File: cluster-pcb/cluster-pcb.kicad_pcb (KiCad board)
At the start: 4 copper layers, 60 x 160 mm, 103 parts, among them J1001 Conn_01x04_P3.5mm_TBH_Horizon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, J1101 Conn_01x04_P3.5mm_TBH_Horizon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, J501 Conn_01x04_P3.5mm_TBH_Horizon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, J601 Conn_01x04_P3.5mm_TBH_Horizon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, J701 Conn_01x04_P3.5mm_TBH_Horizon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, J801 Conn_01x04_P3.5mm_TBH_Horizon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, J901 Conn_01x04_P3.5mm_TBH_Horizon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, SW1201 SW_DIP_x08_SDA08H1SBDR, T301 TERM_BLK_HDR_2POS_90DEG_0.2IN, U1001 Interface_RS485_MAX13431E, U1002 TPS1H200AQDGNRQ1, U1101 Interface_RS485_MAX13431E, U1102 TPS1H200AQDGNRQ1, U1201 TCA6408ARGTR, U1301 MUX507, U1401 TPA6204A1DRBR, U301 TPSM365R6V5RDNR, U501 Interface_RS485_MAX13431E, U502 TPS1H200AQDGNRQ1, U601 Interface_RS485_MAX13431E, U602 TPS1H200AQDGNRQ1, U701 Interface_RS485_MAX13431E, U702 TPS1H200AQDGNRQ1, U801 Interface_RS485_MAX13431E, U802 TPS1H200AQDGNRQ1, U901 Interface_RS485_MAX13431E, U902 TPS1H200AQDGNRQ1

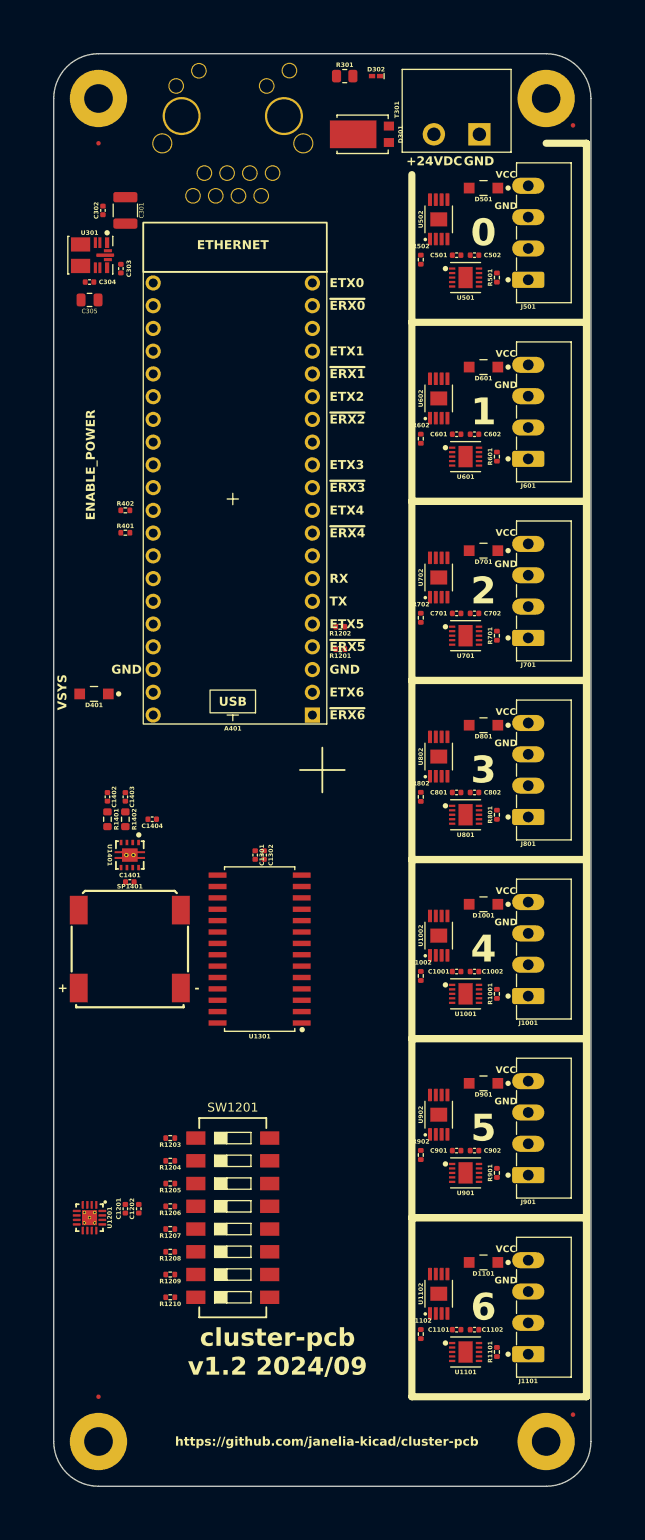
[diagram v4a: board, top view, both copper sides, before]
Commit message: Routed most tracks
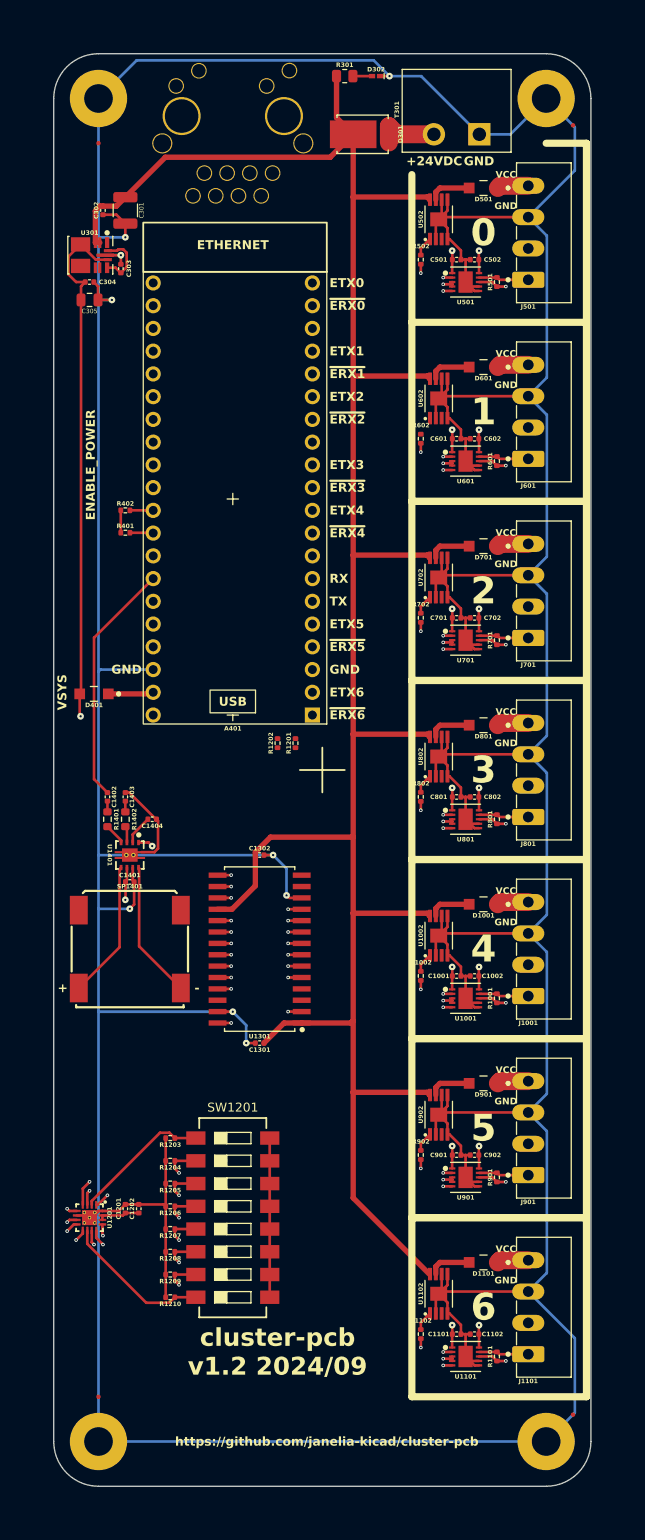
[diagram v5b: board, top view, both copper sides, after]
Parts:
- C1301: value 0.1uF_100V -> 1uF_35V
- moved C1301 21.0 mm to (95.4, 132.1), turned to 180 degrees
- moved R1202 14.8 mm to (97.4, 98.6), turned to 90 degrees
- moved R1201 11.6 mm to (99.4, 98.6), turned to 90 degrees
- moved C1001 0.50 mm to (117.4, 124.6)
- moved C1002 0.50 mm to (119.4, 124.6)
- moved C1101 0.50 mm to (117.4, 164.6)
- moved C1102 0.50 mm to (119.4, 164.6)
- moved C1302 0.50 mm to (95.4, 111.1), turned to 0 degrees
- moved C501 0.50 mm to (117.4, 44.6)
- moved C502 0.50 mm to (119.4, 44.6)
- moved C601 0.50 mm to (117.4, 64.6)
- moved C602 0.50 mm to (119.4, 64.6)
- moved C701 0.50 mm to (117.4, 84.6)
- moved C702 0.50 mm to (119.4, 84.6)
- moved C801 0.50 mm to (117.4, 104.6)
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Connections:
- A401 pad 1: unconnected-(A401-UART0-TX/I2C0-SDA/SPI0-RX/GP0-Pad1) -> /~{ADDRESS_RESET}
- A401 pad 10: /MUX_ADDRESS_1 -> unconnected-(A401-I2C1-SCL/SPI0-TX/GP7-Pad10)
- A401 pad 11: /MUX_ADDRESS_0 -> /ENABLE_TXRX_6
- A401 pad 12: /ENABLE_TXRX_6 -> /ENABLE_TXRX_5
- A401 pad 14: /ENABLE_TXRX_5 -> /ENABLE_TXRX_4
- A401 pad 15: /ENABLE_TXRX_4 -> /ENABLE_TXRX_3
- A401 pad 16: /ENABLE_TXRX_3 -> /ENABLE_TXRX_2
- A401 pad 17: /ENABLE_TXRX_2 -> /ENABLE_TXRX_1
- A401 pad 19: /ENABLE_TXRX_1 -> /ENABLE_TXRX_0
- A401 pad 2: unconnected-(A401-UART0-RX/I2C0-SCL/SPI0-CS/GP1-Pad2) -> /~{ADDRESS_INT}
- A401 pad 20: /ENABLE_TXRX_0 -> /ENABLE_POWER
- A401 pad 29: /ENABLE_POWER -> unconnected-(A401-GP22-Pad29)
- A401 pad 4: /~{ADDRESS_RESET} -> /MUX_ADDRESS_2
- A401 pad 5: /~{ADDRESS_INT} -> /MUX_ADDRESS_1
- A401 pad 9: /MUX_ADDRESS_2 -> /MUX_ADDRESS_0
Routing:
- net /GND: track 0.00 -> 759.1 mm, vias 0 -> 9
- net /VAA: track 0.00 -> 258.2 mm
- net /+5V: track 0.00 -> 201.7 mm, vias 0 -> 10
- net /+3.3V: track 0.00 -> 162.6 mm, vias 0 -> 7
- net /ENABLE_POWER: track 0.00 -> 126.9 mm, vias 0 -> 7
- net /address/P3: track 0.00 -> 35.5 mm, vias 0 -> 2
- net /address/P4: track 0.00 -> 29.7 mm, vias 0 -> 2
- net /AUDIO: track 0.00 -> 27.3 mm
- net /address/P5: track 0.00 -> 24.4 mm, vias 0 -> 2
- net /address/P6: track 0.00 -> 18.6 mm, vias 0 -> 2
- net /address/P2: track 0.00 -> 17.8 mm, vias 0 -> 2
- net /address/P1: track 0.00 -> 17.8 mm, vias 0 -> 2
- net /address/P7: track 0.00 -> 16.6 mm
- net /address/P0: track 0.00 -> 15.5 mm
- net /audio/VO+: track 0.00 -> 15.4 mm
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
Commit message: Update to version 1.2
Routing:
- net /+3.3V: track 162.6 -> 273.3 mm, vias 7 -> 10
- net /ENABLE_TXRX_6: track 1.50 -> 107.0 mm, vias 1 -> 2
- net /TX_0: track 2.53 -> 94.3 mm, vias 2 -> 3
- net /ENABLE_TXRX_5: track 1.50 -> 88.1 mm, vias 1 -> 2
- net /SDA: track 3.88 -> 87.3 mm, vias 1 -> 2
- net /SCL: track 4.49 -> 87.4 mm, vias 1 -> 2
- net /RX_0: track 2.53 -> 84.8 mm, vias 2 -> 3
- net /~{ADDRESS_INT}: track 1.67 -> 82.0 mm
- net /ENABLE_TXRX_4: track 1.50 -> 78.1 mm, vias 1 -> 2
- net /+5V: track 201.7 -> 278.1 mm
- net /~{ADDRESS_RESET}: track 1.69 -> 68.5 mm
- net /RX_1: track 2.53 -> 65.0 mm, vias 2 -> 3
- net /TX_1: track 2.53 -> 64.0 mm, vias 2 -> 3
- net /ENABLE_TXRX_3: track 1.50 -> 59.4 mm, vias 1 -> 2
- net /RX_6: track 2.53 -> 59.4 mm, vias 2 -> 3
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- added copper zone on F.Cu, net /+5V
- added copper zone on B.Cu, net /GND
- added copper zone on In1.Cu, net /GND
- added copper zone on In2.Cu, net /GND
- added copper zone on F.Cu, net /VAA
- added copper zone on F.Cu, net /power/VAA
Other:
- board text added: "+3.3V"
- board text added: "AUDIO"
- board text added: "EN_POWER"
- board text added: "EN_TXRX_0"
- board text added: "EN_TXRX_1"
- board text added: "EN_TXRX_2"
- board text added: "EN_TXRX_3"
- board text added: "EN_TXRX_4"
- board text added: "EN_TXRX_5"
- board text added: "EN_TXRX_6"
- board text added: "MX_ADDR_0"
- board text added: "MX_ADDR_1"
- board text added: "MX_ADDR_2"
- board text added: "SCL"
- board text added: "SDA"
- board text added: "SWN"
- board text added: "SWP"
- board text added: "~{ADDR_INT}"
- board text added: "~{ADDR_RST}"
- board text removed: "ENABLE_POWER"
- board text removed: "ETX0"
- board text removed: "ETX1"
- board text removed: "ETX2"
- board text removed: "ETX3"
- board text removed: "ETX4"
- board text removed: "ETX5"
- board text removed: "ETX6"
- board text removed: "~{ERX0}"
- board text removed: "~{ERX1}"
- board text removed: "~{ERX2}"
- board text removed: "~{ERX3}"
- board text removed: "~{ERX4}"
- board text removed: "~{ERX5}"
- board text removed: "~{ERX6}"

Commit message: Finish routing
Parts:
- J1001, J1101, J501, J601, J701, J801, J901: value Conn_01x04_P3.5mm_TBH_Horizontal_Screw -> Connector_USB_C_Receptacle_USB2.0_16P_GT-USB-7047C; footprint Janelia:PhoenixContact_MC_1,5_4-G-3.5_1x04_P3.50mm_Horizontal_Screw -> Janelia:USB_C_Receptacle_GT-USB-7047C_16P_TopMnt_Horizontal
- R1001, R1101, R501, R601, R701, R801, R901: value 120 -> 100
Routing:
- net /GND: track 766.1 -> 611.5 mm, vias 9 -> 16
- net /prism-0/VCC: track 3.50 -> 11.9 mm
- net /prism-3/VCC: track 3.50 -> 11.8 mm
- net /prism-2/VCC: track 3.50 -> 11.8 mm
- net /prism-4/VCC: track 3.50 -> 11.7 mm
- net /prism-6/VCC: track 3.50 -> 11.7 mm
- net /prism-5/VCC: track 3.50 -> 11.7 mm
- net /prism-1/VCC: track 3.50 -> 11.7 mm
- net /prism-3/SWN: track 5.61 -> 10.6 mm, vias 0 -> 2
- net /prism-0/SWN: track 5.61 -> 10.6 mm, vias 0 -> 2
- net /prism-6/SWN: track 5.61 -> 10.6 mm, vias 0 -> 2
- net /prism-5/SWN: track 5.61 -> 10.6 mm, vias 0 -> 2
- net /prism-1/SWN: track 5.61 -> 10.6 mm, vias 0 -> 2
- net /prism-4/SWN: track 5.61 -> 10.6 mm, vias 0 -> 2
- net /prism-2/SWN: track 5.61 -> 10.6 mm, vias 0 -> 2
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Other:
- board text added: "RS-485 UART half duplex 24V OUT"
- board text added: "cluster-pcb v1.3 2024/10"
- board text removed: "SWN"
- board text removed: "SWP"
- board text removed: "VCC"
- board text removed: "cluster-pcb v1.2 2024/09"
